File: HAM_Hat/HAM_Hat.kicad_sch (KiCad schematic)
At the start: 48 parts, among them J101 TL212V-02P-G12S, J102 DB-9RS-C, J103 NCW254-02S, J104 SMA6252A2, J109 socket, J3 FHDH2.54-40, M101 Fan, Q101 BSS138, Q102 BSS138, Q103 BSS138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

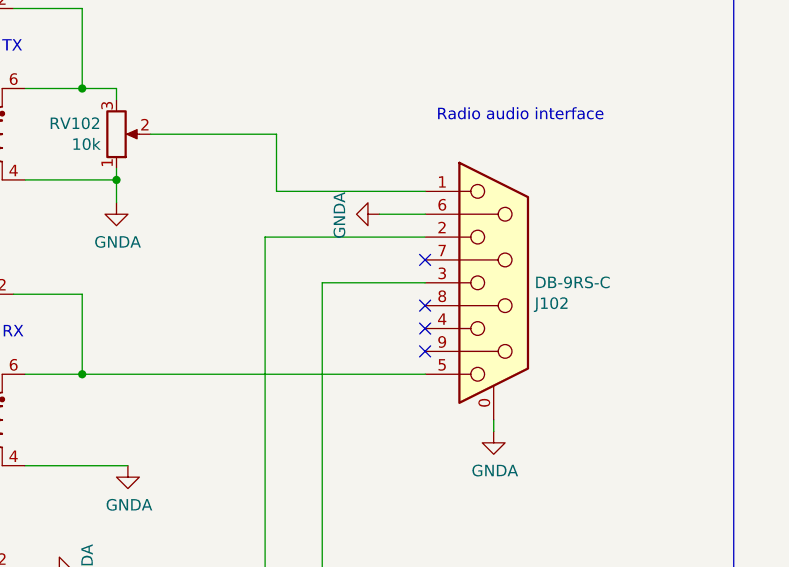
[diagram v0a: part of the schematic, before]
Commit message: Connect more GND to the connector
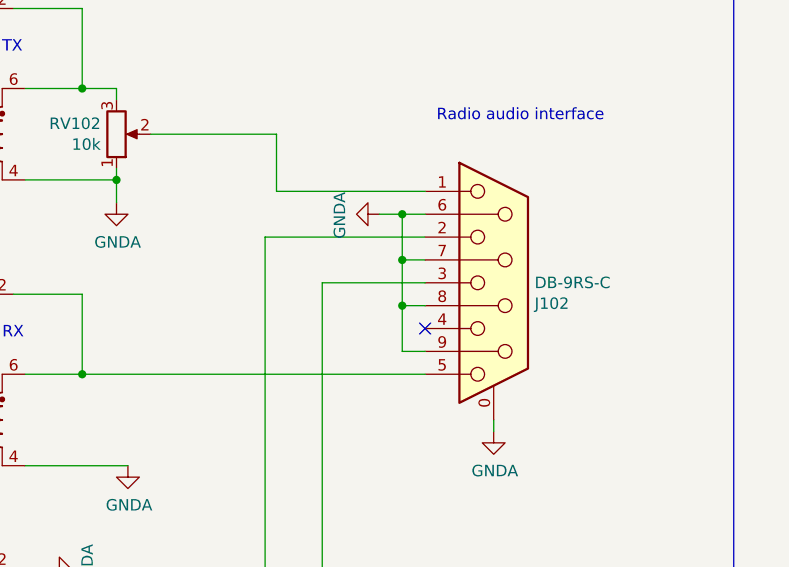
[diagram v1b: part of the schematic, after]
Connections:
- net GNDA: now also J102.7, J102.8, J102.9
- no-connect marks 34 -> 31
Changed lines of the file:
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@@
   (junction (at 262.89 60.96) (diameter 0) (color 0 0 0 0)
   )
+  (junction (at 358.14 121.92) (diameter 0) (color 0 0 0 0)
+  )
   (junction (at 165.1 163.83) (diameter 0) (color 0 0 0 0)
   )
@@
   (junction (at 62.23 170.18) (diameter 0) (color 0 0 0 0)
   )
+  (junction (at 358.14 127) (diameter 0) (color 0 0 0 0)
+  )
   (junction (at 322.58 134.62) (diameter 0) (color 0 0 0 0)
   )
@@
   )
   (junction (at 151.13 163.83) (diameter 0) (color 0 0 0 0)
+  )
+  (junction (at 358.14 116.84) (diameter 0) (color 0 0 0 0)
   )
   (junction (at 179.07 151.13) (diameter 0) (color 0 0 0 0)
@@
   (no_connect (at 191.77 63.5))
   (no_connect (at 224.79 45.72))
-  (no_connect (at 360.68 127))
   (no_connect (at 81.28 77.47))
   (no_connect (at 50.8 92.71))
   (no_connect (at 69.85 168.91))
   (no_connect (at 50.8 95.25))
-  (no_connect (at 360.68 132.08))
   (no_connect (at 50.8 74.93))
   (no_connect (at 81.28 95.25))
@@
   (no_connect (at 50.8 100.33))
   (no_connect (at 198.12 248.92))
-  (no_connect (at 360.68 121.92))
   (no_connect (at 360.68 129.54))
   (no_connect (at 224.79 43.18))
@@
     (stroke (width 0) (type default))
   )
+  (wire (pts (xy 358.14 127) (xy 360.68 127))
+    (stroke (width 0) (type default))
+  )
   (wire (pts (xy 144.78 45.72) (xy 130.81 45.72))
     (stroke (width 0) (type default))
@@
     (stroke (width 0) (type default))
   )
+  (wire (pts (xy 358.14 121.92) (xy 360.68 121.92))
+    (stroke (width 0) (type default))
+  )
   (wire (pts (xy 135.89 50.8) (xy 135.89 69.85))
     (stroke (width 0) (type default))
@@
     (stroke (width 0) (type default))
   )
+  (wire (pts (xy 358.14 127) (xy 358.14 121.92))
+    (stroke (width 0) (type default))
+  )
   (wire (pts (xy 200.66 163.83) (xy 190.5 163.83))
     (stroke (width 0) (type default))
@@
     (stroke (width 0) (type default))
   )
+  (wire (pts (xy 358.14 132.08) (xy 358.14 127))
+    (stroke (width 0) (type default))
+  )
   (wire (pts (xy 157.48 82.55) (xy 157.48 76.2))
     (stroke (width 0) (type default))
@@
     (stroke (width 0) (type default))
   )
-  (wire (pts (xy 355.6 116.84) (xy 360.68 116.84))
+  (wire (pts (xy 355.6 116.84) (xy 358.14 116.84))
     (stroke (width 0) (type default))
   )
@@
     (stroke (width 0) (type default))
   )
+  (wire (pts (xy 358.14 116.84) (xy 360.68 116.84))
+    (stroke (width 0) (type default))
+  )
   (wire (pts (xy 152.4 234.95) (xy 152.4 251.46))
     (stroke (width 0) (type default))
   )
+  (wire (pts (xy 358.14 121.92) (xy 358.14 116.84))
+    (stroke (width 0) (type default))
+  )
   (wire (pts (xy 318.77 170.18) (xy 349.25 170.18))
     (stroke (width 0) (type default))
@@
     (stroke (width 0) (type default))
   )
+  (wire (pts (xy 360.68 132.08) (xy 358.14 132.08))
+    (stroke (width 0) (type default))
+  )

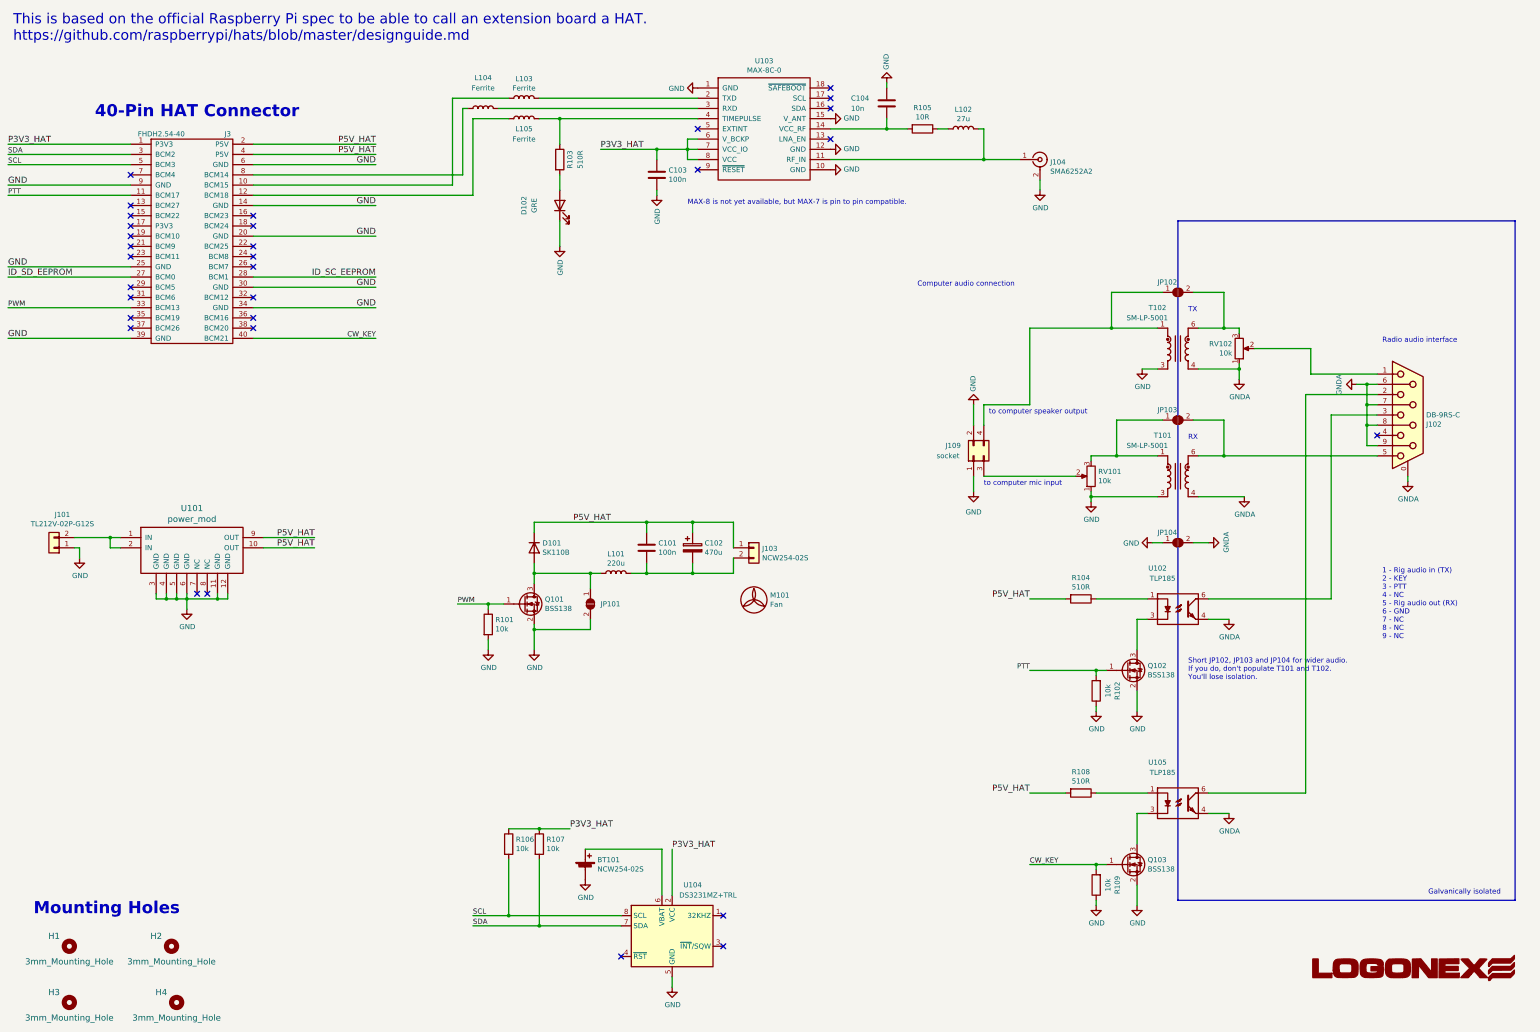
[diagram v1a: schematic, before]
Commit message: Migration to KiCad v8.0.1
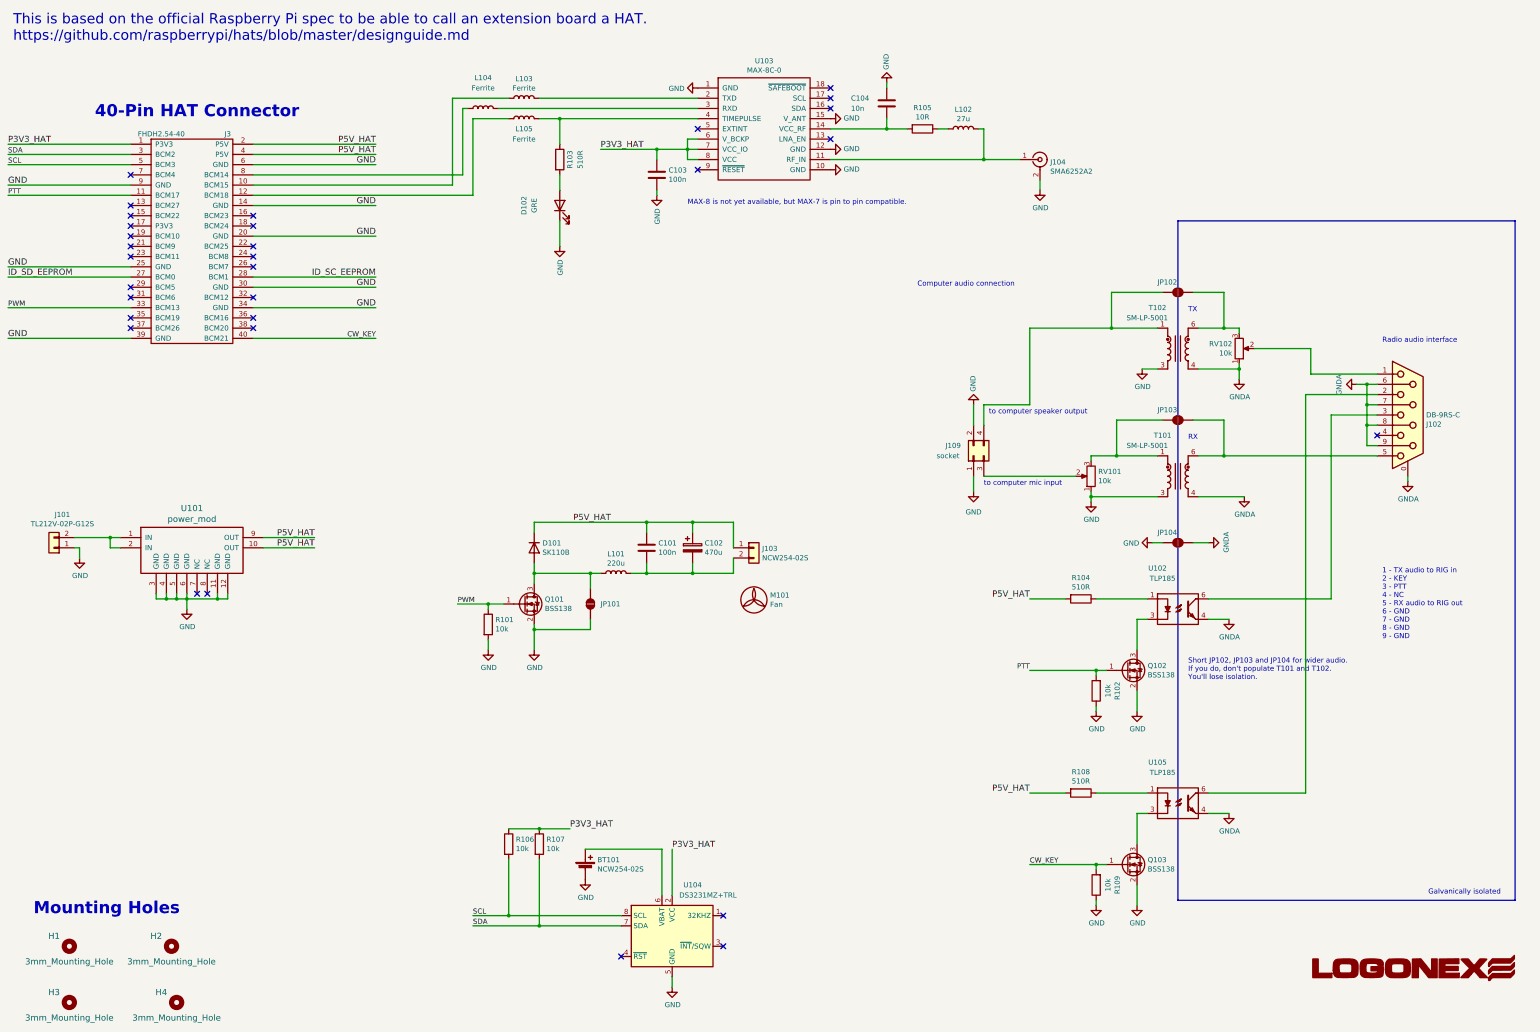
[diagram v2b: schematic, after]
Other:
- note added: "1 - TX audio to RIG in 2 - KEY 3 - PTT 4 - NC 5 - RX audio to RIG out 6 - GND 7 - GND 8 - GND 9 - GND"
- note removed: "1 - Rig audio in (TX) 2 - KEY 3 - PTT 4 - NC 5 - Rig audio out (RX) 6 - GND 7 - NC 8 - NC 9 - NC"

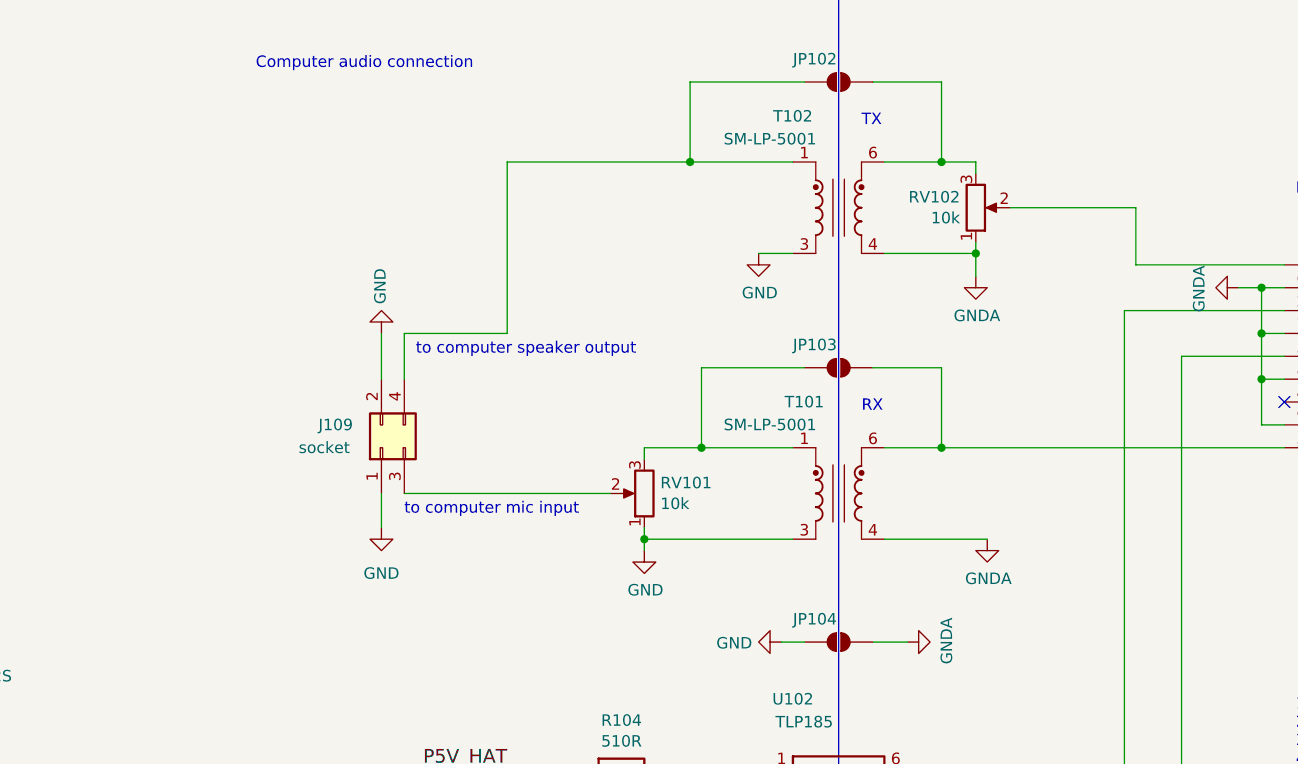
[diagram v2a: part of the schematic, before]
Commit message: Remove the potmeters. Add more robust connector
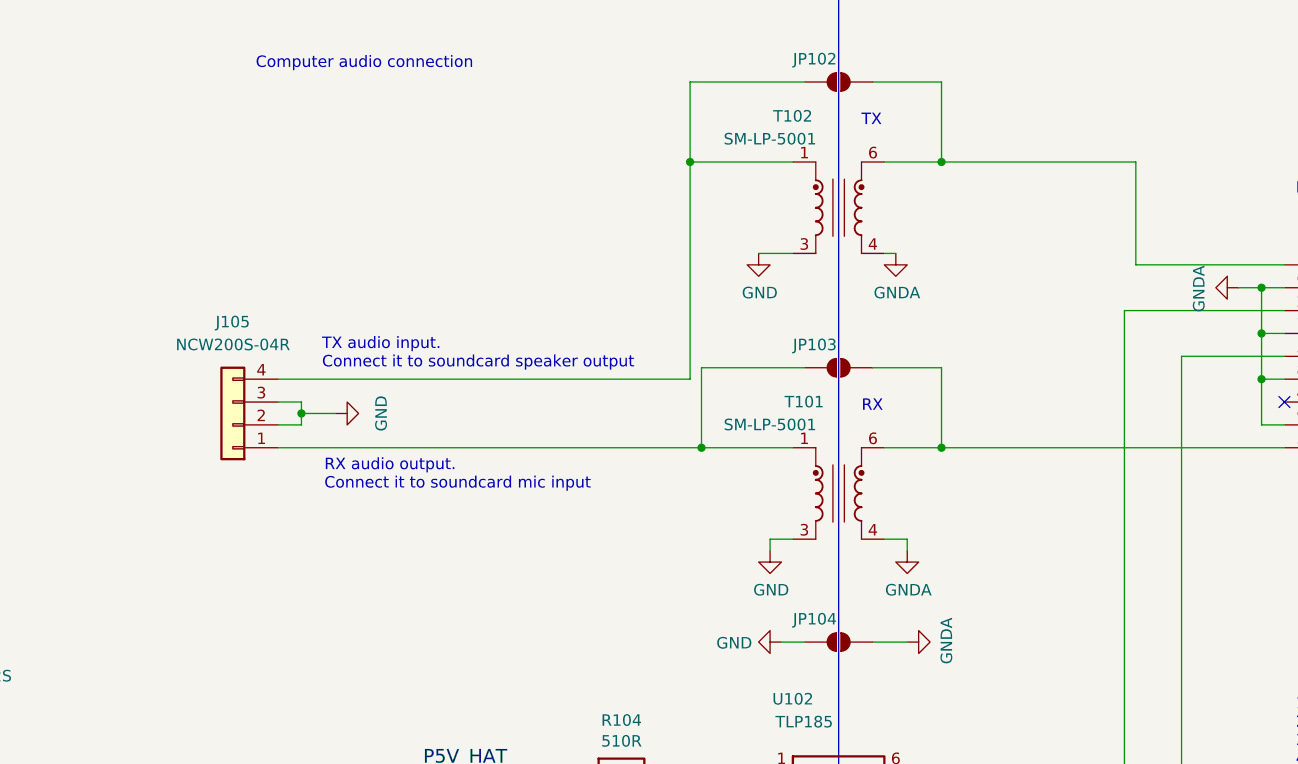
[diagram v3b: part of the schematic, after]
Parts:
- removed J109: socket, Connector_PinSocket_2.54mm:PinSocket_2x02_P2.54mm_Vertical, symbol Connector_Generic:Conn_02x02_Odd_Even
- removed RV101, RV102: 10k, Potentiometer_THT:Potentiometer_Bourns_3296W_Vertical, symbol Device:R_Potentiometer
- added J105: NCW200S-04R, Connector_JST:JST_PH_B4B-PH-K_1x04_P2.00mm_Vertical, symbol default:levcsi_database/459
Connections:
- net GND: now also J105.2 (Pin_2), J105.3 (Pin_3)
- net at J102.1: now also JP102.2 (B), T102.6
- net at JP103.1 (A), T101.1: now also J105.1 (Pin_1)
- net at JP102.1 (A), T102.1: now also J105.4 (Pin_4)
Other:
- note added: "RX audio output. Connect it to soundcard mic input"
- note added: "TX audio input. Connect it to soundcard speaker output"
- note removed: "to computer mic input"
- note removed: "to computer speaker output"

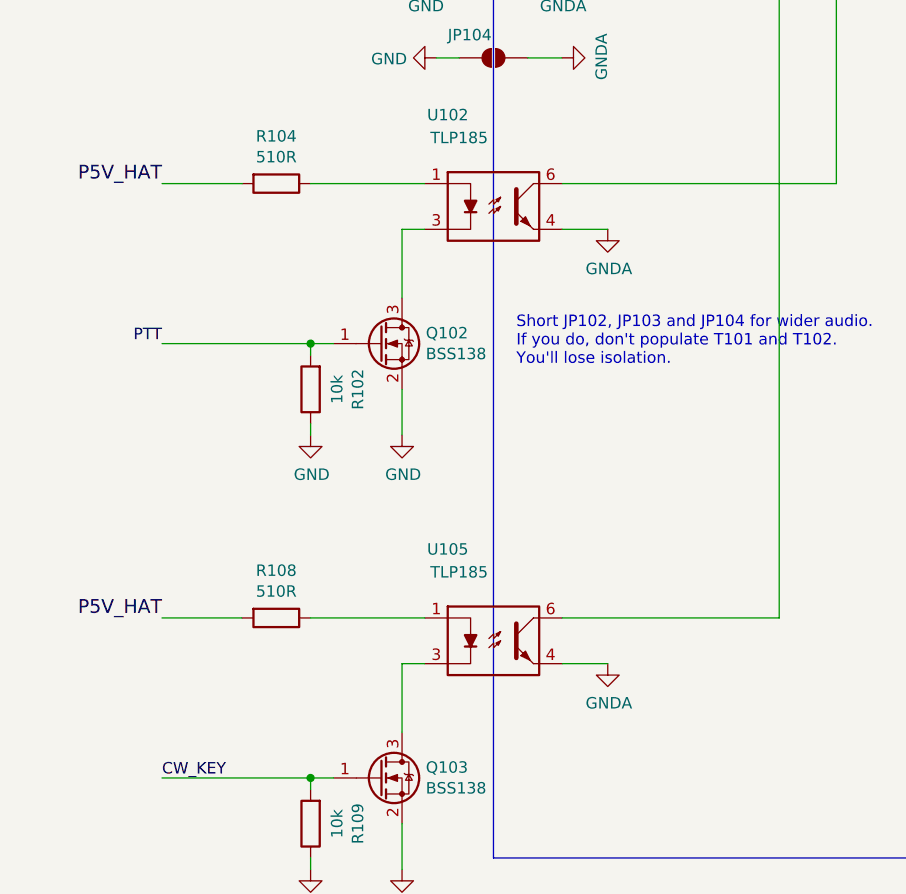
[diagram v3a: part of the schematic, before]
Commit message: Add LEDs to CW and PTT lines
Rotate the GPS module
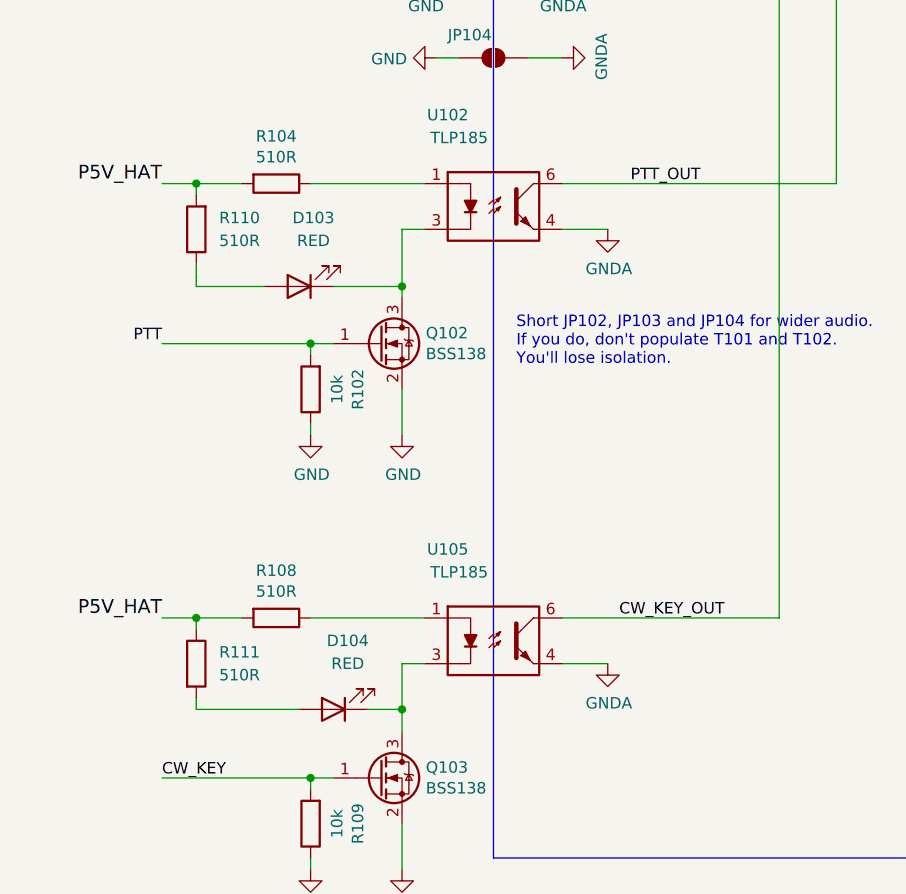
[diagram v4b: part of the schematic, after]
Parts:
- added D103, D104: RED, LED_SMD:LED_0603_1608Metric, symbol default:levcsi_database/258
- added R110, R111: 510R, Resistor_SMD:R_0603_1608Metric, symbol default:levcsi_database/390
- J104: footprint l_rf:SMA_angled -> Connector_Coaxial:U.FL_Molex_MCRF_73412-0110_Vertical; id 658 -> (none)
- T101, T102: footprint l_transformer:SM_LP_5001 -> Transformer_SMD:Pulse_PA2006NL
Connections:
- net P5V_HAT: now also R110.2, R111.1
- net CW_KEY_OUT: now reaches J102.2, U105.6
- net PTT_OUT: now reaches J102.3, U102.6
- net at Q102.3 (D), U102.3: now also D103.1 (K)
- net at Q103.3 (D), U105.3: now also D104.1 (K)
- new net: D104.2 (A), R111.2
- new net: D103.2 (A), R110.1
